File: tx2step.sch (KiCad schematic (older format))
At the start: 68 parts, among them CON1 BARREL_JACK, IC1 TPS2113A, IC2 ATMEGA328P-MM, IC3 MCP73831, IC4 TPS61202, IC5 DRV8834, IC6 DRV8834, J1 8P8C, J2 6P4C, J3 6P4C, J4 Debug, SW1 SW_DIP_x02, SW2 SW_DPDT_x2, SW3 SW_SPDT_MSM, Y1 16 MHz

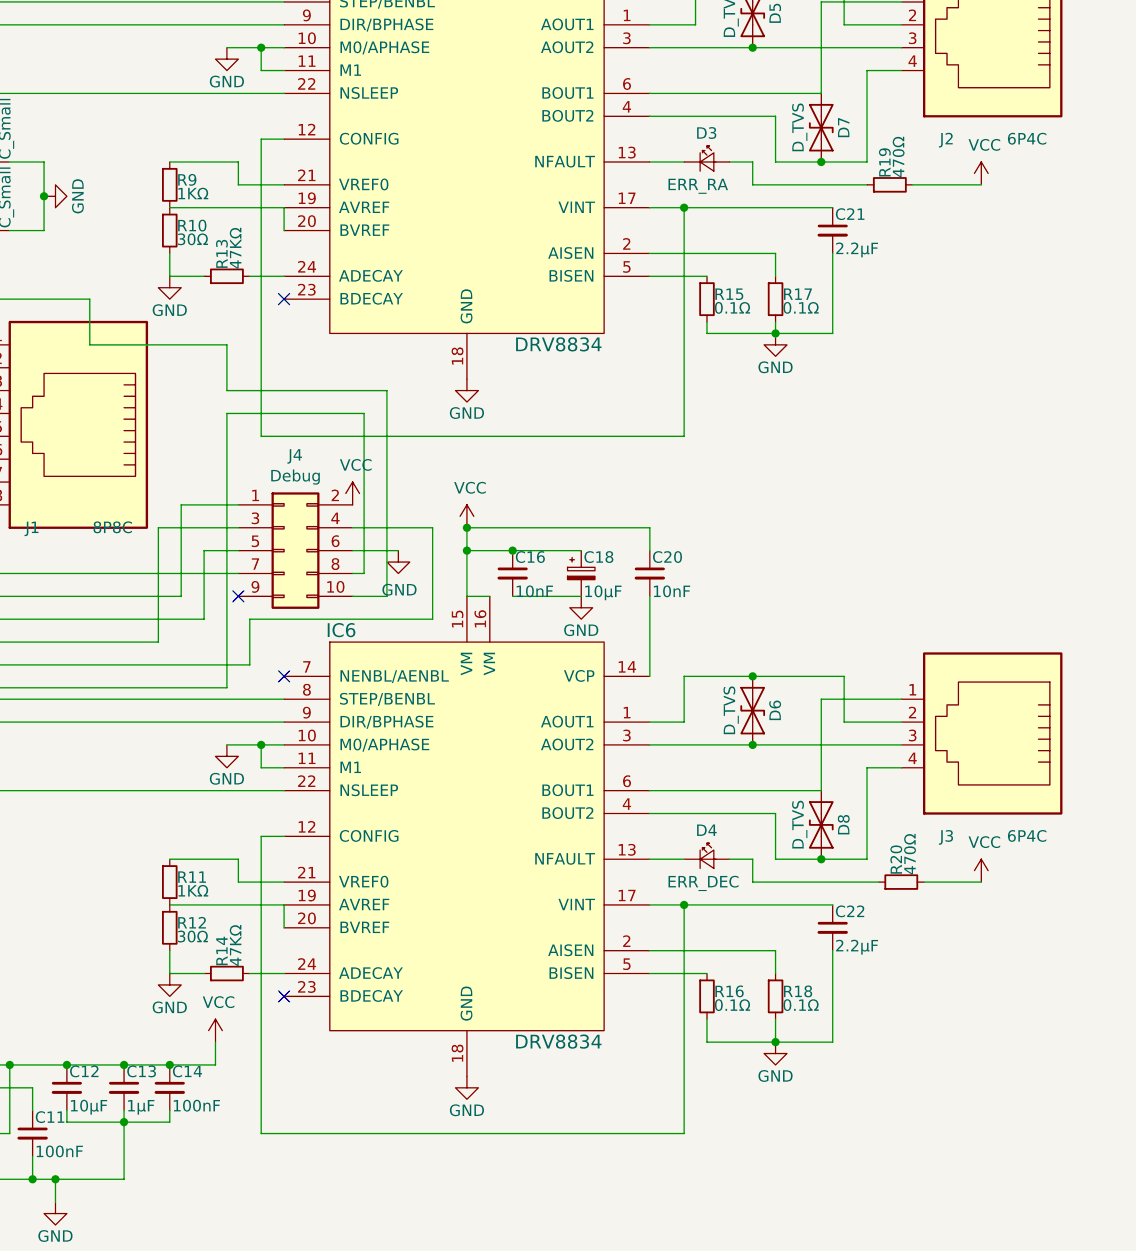
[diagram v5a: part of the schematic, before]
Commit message: Simplify DRV8834 current limit configuration
Wire A/B VREF directly to VREFO and connect the ISEN pins to a
resistor network. The current limiting can be adjusted by swapping
the resistor value.
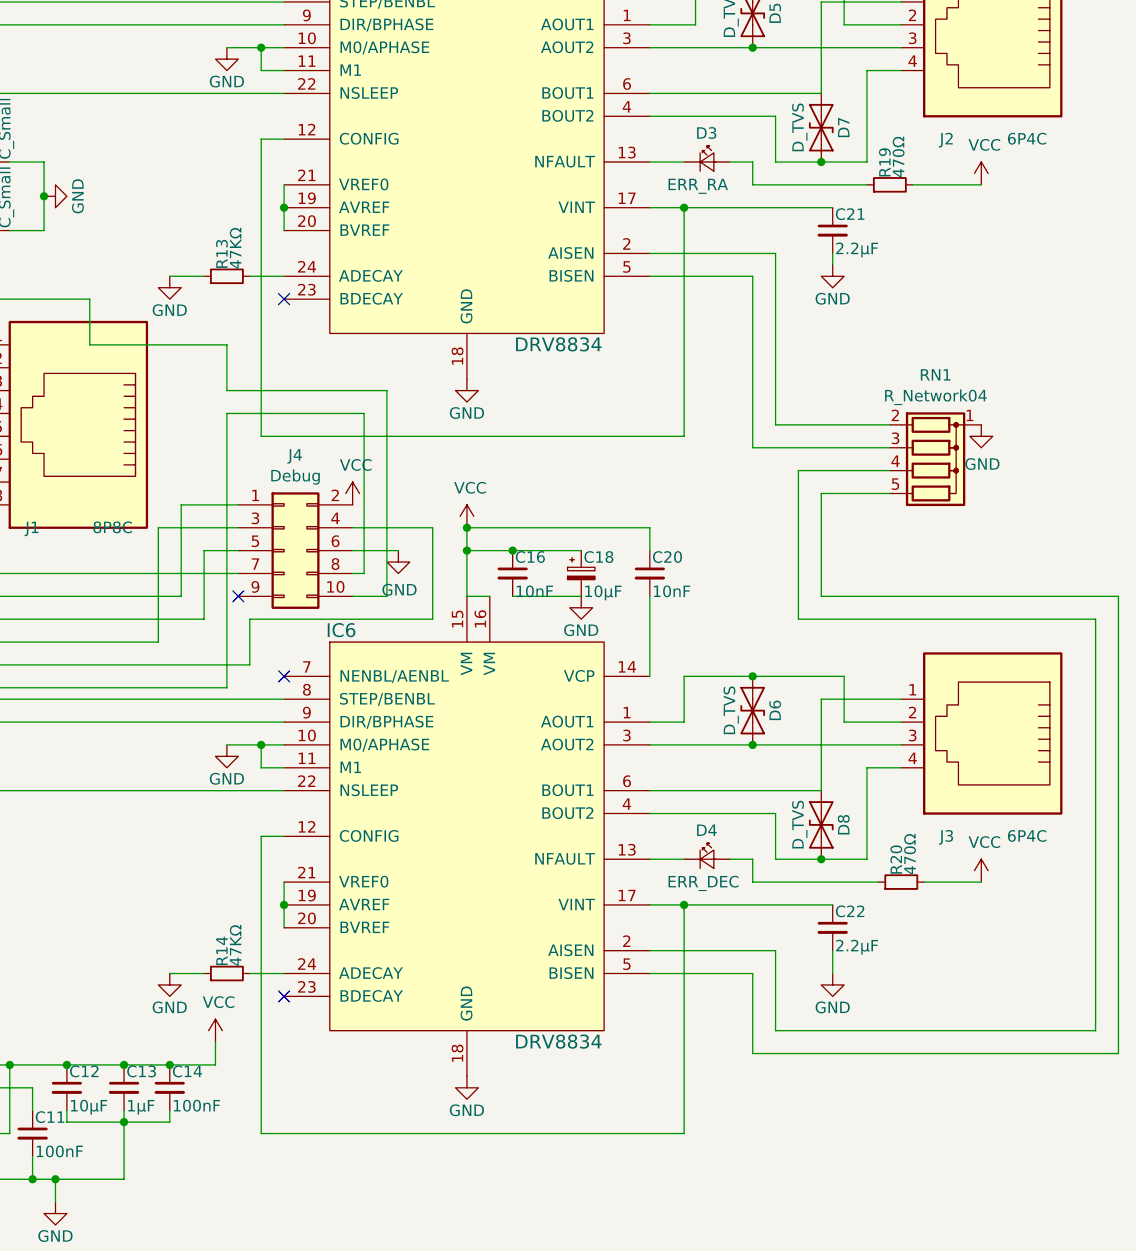
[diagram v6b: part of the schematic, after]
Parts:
- removed R10, R12: 30Ω, symbol tx2step-rescue:R_Small
- removed R11, R9: 1KΩ, symbol tx2step-rescue:R_Small
- removed R15, R16, R17, R18: 0.1Ω, symbol tx2step-rescue:R_Small
- added RN1: R_Network04, Resistor_THT:R_Array_SIP5, symbol Device:R_Network04
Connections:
- net GND: now also RN1.1 (common)
- net at IC5.19 (AVREF), IC5.20 (BVREF): now also IC5.21 (VREF0)
- net at IC5.2 (AISEN): now also RN1.2 (R1)
- net at IC5.5 (BISEN): now also RN1.3 (R2)
- net at IC6.19 (AVREF), IC6.20 (BVREF): now also IC6.21 (VREF0)
- net at IC6.2 (AISEN): now also RN1.4 (R3)
- net at IC6.5 (BISEN): now also RN1.5 (R4)
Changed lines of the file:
@@
-$EndComp
-$Comp
-L tx2step-rescue:R_Small R15
-U 1 1 58B98502
-P 8550 2950
-F 0 "R15" H 8580 2970 50  0000 L CNN
-F 1 "0.1Ω" H 8580 2910 50  0000 L CNN
-F 2 "" H 8550 2950 50  0000 C CNN
-F 3 "" H 8550 2950 50  0000 C CNN
-	1    8550 2950
-	1    0    0    -1
-$EndComp
-$Comp
-L tx2step-rescue:R_Small R17
-U 1 1 58B98573
-P 8850 2950
-F 0 "R17" H 8880 2970 50  0000 L CNN
-F 1 "0.1Ω" H 8880 2910 50  0000 L CNN
-F 2 "" H 8850 2950 50  0000 C CNN
-F 3 "" H 8850 2950 50  0000 C CNN
-	1    8850 2950
-	1    0    0    -1
 $EndComp
 $Comp
 L tx2step-rescue:GND #PWR038
 U 1 1 58B9897E
-P 8850 3100
-F 0 "#PWR038" H 8850 2850 50  0001 C CNN
-F 1 "GND" H 8850 2950 50  0000 C CNN
-F 2 "" H 8850 3100 50  0000 C CNN
-F 3 "" H 8850 3100 50  0000 C CNN
-	1    8850 3100
-	1    0    0    -1
-$EndComp
-$Comp
-L tx2step-rescue:R_Small R16
-U 1 1 58B98E8F
-P 8550 6000
-F 0 "R16" H 8580 6020 50  0000 L CNN
-F 1 "0.1Ω" H 8580 5960 50  0000 L CNN
-F 2 "" H 8550 6000 50  0000 C CNN
-F 3 "" H 8550 6000 50  0000 C CNN
-	1    8550 6000
-	1    0    0    -1
-$EndComp
-$Comp
-L tx2step-rescue:R_Small R18
-U 1 1 58B98F26
-P 8850 6000
-F 0 "R18" H 8880 6020 50  0000 L CNN
-F 1 "0.1Ω" H 8880 5960 50  0000 L CNN
-F 2 "" H 8850 6000 50  0000 C CNN
-F 3 "" H 8850 6000 50  0000 C CNN
-	1    8850 6000
+P 9100 2800
+F 0 "#PWR038" H 9100 2550 50  0001 C CNN
+F 1 "GND" H 9100 2650 50  0000 C CNN
+F 2 "" H 9100 2800 50  0000 C CNN
+F 3 "" H 9100 2800 50  0000 C CNN
+	1    9100 2800
 	1    0    0    -1
 $EndComp
@@
 L tx2step-rescue:GND #PWR039
 U 1 1 58B993B1
-P 8850 6200
-F 0 "#PWR039" H 8850 5950 50  0001 C CNN
-F 1 "GND" H 8850 6050 50  0000 C CNN
-F 2 "" H 8850 6200 50  0000 C CNN
-F 3 "" H 8850 6200 50  0000 C CNN
-	1    8850 6200
+P 9100 5900
+F 0 "#PWR039" H 9100 5650 50  0001 C CNN
+F 1 "GND" H 9100 5750 50  0000 C CNN
+F 2 "" H 9100 5900 50  0000 C CNN
+F 3 "" H 9100 5900 50  0000 C CNN
+	1    9100 5900
 	1    0    0    -1
 $EndComp
@@
 F 3 "" H 9100 2650 50  0000 C CNN
 	1    9100 2650
-	1    0    0    -1
-$EndComp
-$Comp
-L tx2step-rescue:R_Small R9
-U 1 1 58B9B75C
-P 6200 2450
-F 0 "R9" H 6230 2470 50  0000 L CNN
-F 1 "1KΩ" H 6230 2410 50  0000 L CNN
-F 2 "" H 6200 2450 50  0000 C CNN
-F 3 "" H 6200 2450 50  0000 C CNN
-	1    6200 2450
-	1    0    0    -1
-$EndComp
-$Comp
-L tx2step-rescue:R_Small R10
-U 1 1 58B9B7E8
-P 6200 2650
-F 0 "R10" H 6230 2670 50  0000 L CNN
-F 1 "30Ω" H 6230 2610 50  0000 L CNN
-F 2 "" H 6200 2650 50  0000 C CNN
-F 3 "" H 6200 2650 50  0000 C CNN
-	1    6200 2650
-	1    0    0    -1
-$EndComp
-$Comp
-L tx2step-rescue:R_Small R12
-U 1 1 58B9BECE
-P 6200 5700
-F 0 "R12" H 6230 5720 50  0000 L CNN
-F 1 "30Ω" H 6230 5660 50  0000 L CNN
-F 2 "" H 6200 5700 50  0000 C CNN
-F 3 "" H 6200 5700 50  0000 C CNN
-	1    6200 5700
-	1    0    0    -1
-$EndComp
-$Comp
-L tx2step-rescue:R_Small R11
-U 1 1 58B9C30F
-P 6200 5500
-F 0 "R11" H 6230 5520 50  0000 L CNN
-F 1 "1KΩ" H 6230 5460 50  0000 L CNN
-F 2 "" H 6200 5500 50  0000 C CNN
-F 3 "" H 6200 5500 50  0000 C CNN
-	1    6200 5500
 	1    0    0    -1
 $EndComp
@@
 	6200 5900 6350 5900
 Wire Wire Line
-	8550 2850 8300 2850
-Wire Wire Line
 	8300 2750 8850 2750
 Wire Wire Line
-	8850 3050 8850 3100
-Wire Wire Line
-	8550 3100 8850 3100
-Wire Wire Line
-	8850 5900 8850 5800
-Wire Wire Line
 	8850 5800 8300 5800
-Wire Wire Line
-	8300 5900 8550 5900
-Wire Wire Line
-	8550 3100 8550 3050
-Wire Wire Line
-	8550 6100 8550 6200
-Wire Wire Line
-	8550 6200 8850 6200
-Wire Wire Line
-	8850 6200 8850 6100
 Connection ~ 8450 5600
-Wire Wire Line
-	9100 6200 9100 5800
-Connection ~ 8850 6200
 Connection ~ 8450 2550
 Wire Wire Line
-	9100 3100 9100 2750
-Connection ~ 8850 3100
-Wire Wire Line
-	6700 2450 6500 2450
-Wire Wire Line
-	6500 2450 6500 2350
-Wire Wire Line
-	6500 2350 6200 2350
-Wire Wire Line
-	6200 2550 6700 2550
-Wire Wire Line
 	6700 2550 6700 2650
 Wire Wire Line
-	6200 2850 6200 2750
-Wire Wire Line
-	6200 5600 6700 5600
-Wire Wire Line
 	6700 5600 6700 5700
-Wire Wire Line
-	6700 5500 6500 5500
-Wire Wire Line
-	6500 5500 6500 5400
-Wire Wire Line
-	6500 5400 6200 5400
-Wire Wire Line
-	6200 5800 6200 5900
-Wire Wire Line
-	8850 2750 8850 2850
 Wire Wire Line
 	1100 5550 2250 5550
@@
 	8450 5600 9100 5600
 Wire Wire Line
-	8850 6200 9100 6200
-Wire Wire Line
 	8450 2550 9100 2550
-Wire Wire Line
-	8850 3100 9100 3100
 Wire Wire Line
 	1350 5200 1500 5200
@@
 	7150 4250 7000 4250
 Connection ~ 5400 3050
+Wire Wire Line
+	6700 2550 6700 2450
+Connection ~ 6700 2550
+Wire Wire Line
+	6700 5500 6700 5600
+Connection ~ 6700 5600
+$Comp
+L Device:R_Network04 RN1
+U 1 1 601700D9
+P 9550 3700
+F 0 "RN1" V 9133 3700 50  0000 C CNN
+F 1 "R_Network04" V 9224 3700 50  0000 C CNN
+F 2 "Resistor_THT:R_Array_SIP5" V 9825 3700 50  0001 C CNN
+F 3 "http://www.vishay.com/docs/31509/csc.pdf" H 9550 3700 50  0001 C CNN
+	1    9550 3700
+	0    1    1    0
+$EndComp
+$Comp
+L power:GND #PWR044
+U 1 1 60193DA1
+P 9750 3500
+F 0 "#PWR044" H 9750 3250 50  0001 C CNN
+F 1 "GND" H 9755 3327 50  0000 C CNN
+F 2 "" H 9750 3500 50  0001 C CNN
+F 3 "" H 9750 3500 50  0001 C CNN
+	1    9750 3500
+	1    0    0    -1
+$EndComp
+Wire Wire Line
+	9100 2800 9100 2750
+Wire Wire Line
+	9350 3500 8850 3500
+Wire Wire Line
+	8850 2750 8850 3500
+Wire Wire Line
+	8750 2850 8750 3600
+Wire Wire Line
+	8750 3600 9350 3600
+Wire Wire Line
+	8300 2850 8750 2850
+Wire Wire Line
+	9100 5900 9100 5800
+Wire Wire Line
+	8850 6150 10250 6150
+Wire Wire Line
+	10250 6150 10250 4350
+Wire Wire Line
+	10250 4350 8950 4350
+Wire Wire Line
+	8950 4350 8950 3700
+Wire Wire Line
+	8950 3700 9350 3700
+Wire Wire Line
+	8850 5800 8850 6150
+Wire Wire Line
+	9350 3800 9050 3800
+Wire Wire Line
+	9050 3800 9050 4250
+Wire Wire Line
+	9050 4250 10350 4250
+Wire Wire Line
+	10350 4250 10350 6250
+Wire Wire Line
+	10350 6250 8750 6250
+Wire Wire Line
+	8750 6250 8750 5900
+Wire Wire Line
+	8300 5900 8750 5900
 $EndSCHEMATC

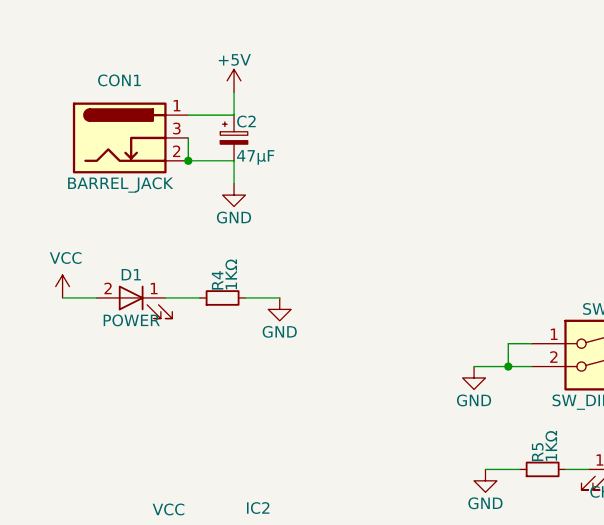
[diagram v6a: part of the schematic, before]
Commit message: Use DC jack switch for LED
Repurpose power LED for use as a "running on battery" indicator.
If the unit is running while plugged in, the charge indicator will
indicate power.
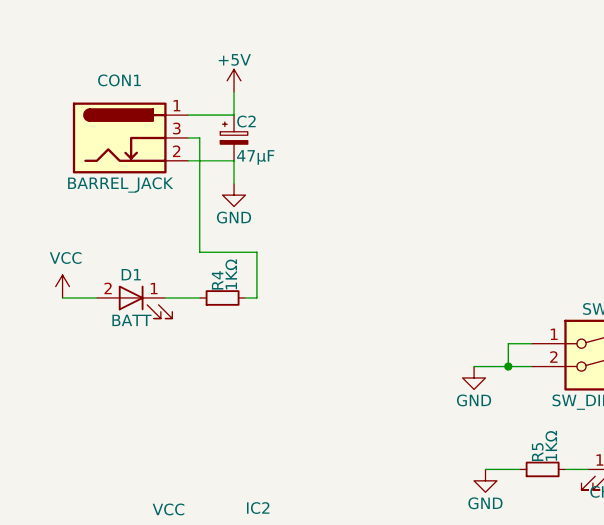
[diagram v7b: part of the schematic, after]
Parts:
- D1: value POWER -> BATT
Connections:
- net GND: no longer CON1.3, R4.2
- new net: CON1.3, R4.2
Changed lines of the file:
@@
-$EndComp
-$Comp
-L tx2step-rescue:R_Small R7
-U 1 1 58B876D6
-P 4700 900
-F 0 "R7" H 4730 920 50  0000 L CNN
-F 1 "4.7KΩ" H 4730 860 50  0000 L CNN
-F 2 "" H 4700 900 50  0000 C CNN
-F 3 "" H 4700 900 50  0000 C CNN
-	1    4700 900
-	1    0    0    -1
-$EndComp
-$Comp
-L tx2step-rescue:R_Small R8
-U 1 1 58B87737
-P 4700 1100
-F 0 "R8" H 4730 1120 50  0000 L CNN
-F 1 "4.7KΩ" H 4730 1060 50  0000 L CNN
-F 2 "" H 4700 1100 50  0000 C CNN
-F 3 "" H 4700 1100 50  0000 C CNN
-	1    4700 1100
-	1    0    0    -1
-$EndComp
-$Comp
-L tx2step-rescue:GND #PWR020
-U 1 1 58B895AD
-P 4700 1200
-F 0 "#PWR020" H 4700 950 50  0001 C CNN
-F 1 "GND" H 4700 1050 50  0000 C CNN
-F 2 "" H 4700 1200 50  0000 C CNN
-F 3 "" H 4700 1200 50  0000 C CNN
-	1    4700 1200
-	1    0    0    -1
 $EndComp
 $Comp
@@
 P 1150 1800
 F 0 "D1" H 1150 1900 50  0000 C CNN
-F 1 "POWER" H 1150 1700 50  0000 C CNN
+F 1 "BATT" H 1150 1700 50  0000 C CNN
 F 2 "" H 1150 1800 50  0000 C CNN
 F 3 "" H 1150 1800 50  0000 C CNN
@@
 $EndComp
 $Comp
-L tx2step-rescue:GND #PWR09
-U 1 1 58B818DF
-P 1800 1800
-F 0 "#PWR09" H 1800 1550 50  0001 C CNN
-F 1 "GND" H 1800 1650 50  0000 C CNN
-F 2 "" H 1800 1800 50  0000 C CNN
-F 3 "" H 1800 1800 50  0000 C CNN
-	1    1800 1800
-	1    0    0    -1
-$EndComp
-$Comp
 L tx2step-rescue:LED_Small D3
 U 1 1 58B8427E
@@
 	5450 1200 5700 1200
 Wire Wire Line
-	4600 1000 4700 1000
-Wire Wire Line
 	4600 3950 3400 3950
-Connection ~ 4700 1000
 Wire Wire Line
 	4100 4050 3400 4050
@@
 	1300 1800 1450 1800
 Wire Wire Line
-	1650 1800 1800 1800
-Wire Wire Line
 	8450 2350 8300 2350
 Wire Wire Line
@@
 	8750 1550 9150 1550
 Wire Wire Line
-	4700 1000 4900 1000
-Wire Wire Line
 	5050 2350 5300 2350
 Wire Wire Line
@@
 Wire Wire Line
 	1600 900  1600 1000
-$Comp
-L power:VCC #PWR019
-U 1 1 5FE31F55
-P 4700 800
-F 0 "#PWR019" H 4700 650 50  0001 C CNN
-F 1 "VCC" H 4715 973 50  0000 C CNN
-F 2 "" H 4700 800 50  0001 C CNN
-F 3 "" H 4700 800 50  0001 C CNN
-	1    4700 800
-	1    0    0    -1
-$EndComp
 $Comp
 L power:VCC #PWR024
@@
 	1    0    0    -1
 $EndComp
-Connection ~ 1400 1200
-Wire Wire Line
-	1400 1100 1400 1200
 $Comp
 L Connector:8P8C J1
@@
 Wire Wire Line
 	8300 5900 8750 5900
+$Comp
+L tx2step-rescue:GND #PWR020
+U 1 1 58B895AD
+P 4700 1200
+F 0 "#PWR020" H 4700 950 50  0001 C CNN
+F 1 "GND" H 4700 1050 50  0000 C CNN
+F 2 "" H 4700 1200 50  0000 C CNN
+F 3 "" H 4700 1200 50  0000 C CNN
+	1    4700 1200
+	1    0    0    -1
+$EndComp
+Wire Wire Line
+	4700 1000 4900 1000
+Wire Wire Line
+	4600 1000 4700 1000
+Connection ~ 4700 1000
+$Comp
+L tx2step-rescue:R_Small R8
+U 1 1 58B87737
+P 4700 1100
+F 0 "R8" H 4730 1120 50  0000 L CNN
+F 1 "4.7KΩ" H 4730 1060 50  0000 L CNN
+F 2 "" H 4700 1100 50  0000 C CNN
+F 3 "" H 4700 1100 50  0000 C CNN
+	1    4700 1100
+	1    0    0    -1
+$EndComp
+$Comp
+L power:VCC #PWR019
+U 1 1 5FE31F55
+P 4700 800
+F 0 "#PWR019" H 4700 650 50  0001 C CNN
+F 1 "VCC" H 4715 973 50  0000 C CNN
+F 2 "" H 4700 800 50  0001 C CNN
+F 3 "" H 4700 800 50  0001 C CNN
+	1    4700 800
+	1    0    0    -1
+$EndComp
+$Comp
+L tx2step-rescue:R_Small R7
+U 1 1 58B876D6
+P 4700 900
+F 0 "R7" H 4730 920 50  0000 L CNN
+F 1 "4.7KΩ" H 4730 860 50  0000 L CNN
+F 2 "" H 4700 900 50  0000 C CNN
+F 3 "" H 4700 900 50  0000 C CNN
+	1    4700 900
+	1    0    0    -1
+$EndComp
+Wire Wire Line
+	1400 1100 1450 1100
+Wire Wire Line
+	1450 1100 1450 1600
+Wire Wire Line
+	1450 1600 1700 1600
+Wire Wire Line
+	1700 1600 1700 1800
+Wire Wire Line
+	1700 1800 1650 1800
 $EndSCHEMATC
